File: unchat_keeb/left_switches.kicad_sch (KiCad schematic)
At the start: 54 parts

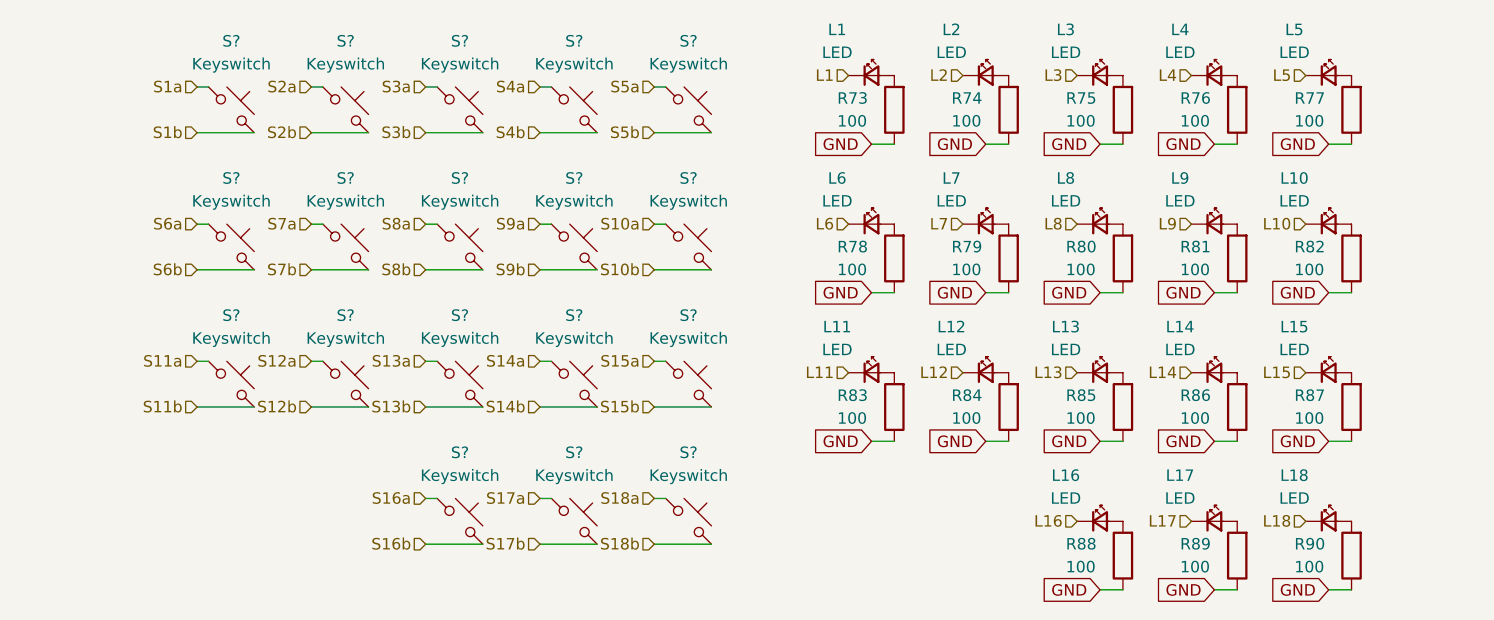
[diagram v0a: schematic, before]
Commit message: Add extra columns, updating to 42-key design
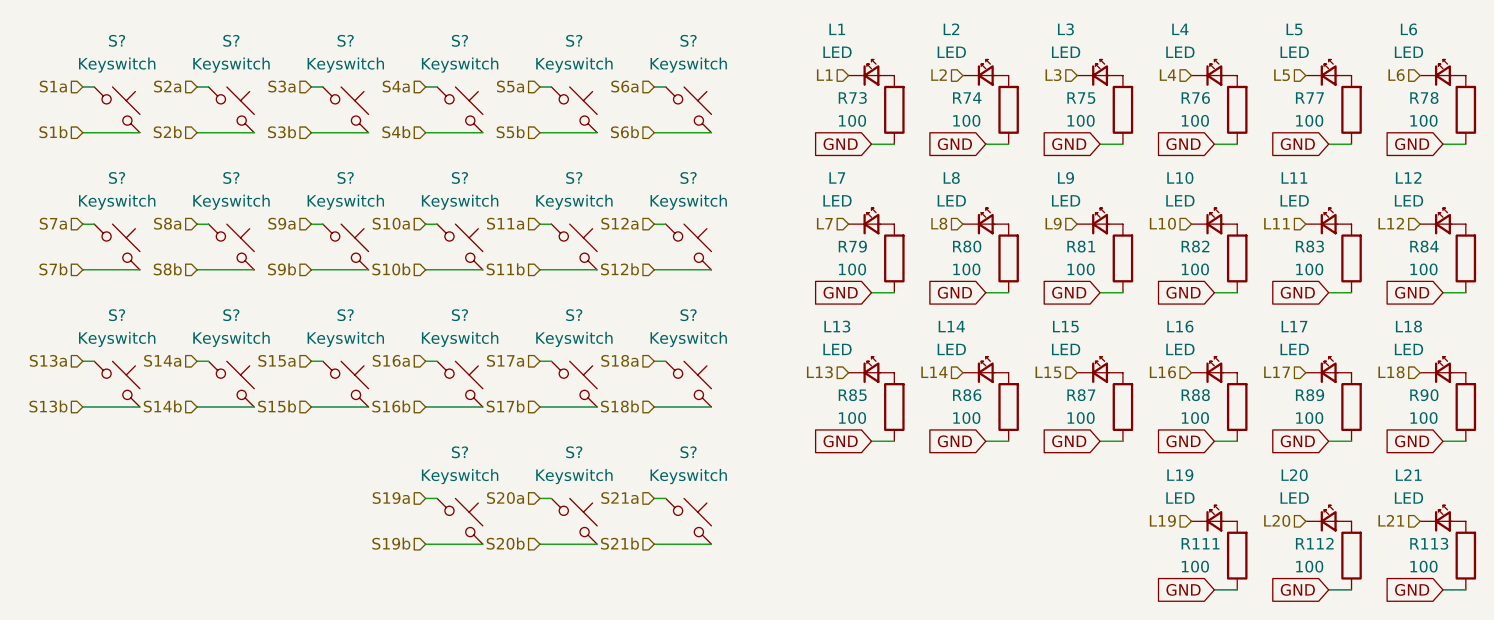
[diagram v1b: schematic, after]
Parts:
- added L1, L13, L7: LED, LED_SMD:LED_0603_1608Metric, symbol Device:LED_Small
- added R73, R79, R85: 100, Resistor_SMD:R_0805_2012Metric, symbol ScottoKeebs:Placeholder_Resistor
- added S? (x3): Keyswitch, GKanwarLibrary:Choc_V1_LED_1.00u, symbol ScottoKeebs:Placeholder_Keyswitch
- renumbered L8 to L10, L9 to L11, L10 to L12, L11 to L14, L12 to L15, L13 to L16, L14 to L17, L15 to L18, L16 to L19, L1 to L2, L17 to L20, L18 to L21, L2 to L3, L3 to L4, L4 to L5, L5 to L6, L6 to L8, L7 to L9, R88 to R111, R89 to R112, R90 to R113, R73 to R74, R74 to R75, R75 to R76, R76 to R77, R77 to R78, R78 to R80, R79 to R81, R80 to R82, R81 to R83, R82 to R84, R83 to R86, R84 to R87, R85 to R88, R86 to R89, R87 to R90
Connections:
- net GND: now also R73.1, R79.1, R85.1
- net L1: now also L1.1 (K); no longer L2.1 (K)
- net L10: now also L10.1 (K); no longer L12.1 (K)
- net L11: now also L11.1 (K); no longer L14.1 (K)
- net L12: now also L12.1 (K); no longer L15.1 (K)
- net L13: now also L13.1 (K); no longer L16.1 (K)
- net L14: now also L14.1 (K); no longer L17.1 (K)
- net L15: now also L15.1 (K); no longer L18.1 (K)
- net L16: now also L16.1 (K); no longer L19.1 (K)
- net L17: now also L17.1 (K); no longer L20.1 (K)
- net L18: now also L18.1 (K); no longer L21.1 (K)
- net L2: now also L2.1 (K); no longer L3.1 (K)
- net L3: now also L3.1 (K); no longer L4.1 (K)
- net L4: now also L4.1 (K); no longer L5.1 (K)
- net L5: now also L5.1 (K); no longer L6.1 (K)
- net L6: now also L6.1 (K); no longer L8.1 (K)
- net L7: now also L7.1 (K); no longer L9.1 (K)
- net L8: now also L8.1 (K); no longer L10.1 (K)
- net L9: now also L9.1 (K); no longer L11.1 (K)
- net S10a: now also S?.1; no longer S?.1
- net S10b: now also S?.2; no longer S?.2
- net S11a: now also S?.1; no longer S?.1
- net S11b: now also S?.2; no longer S?.2
- net S12a: now also S?.1; no longer S?.1
- net S12b: now also S?.2; no longer S?.2
- net S13a: now also S?.1; no longer S?.1
- net S13b: now also S?.2; no longer S?.2
- net S14a: now also S?.1; no longer S?.1
- net S14b: now also S?.2; no longer S?.2
- net S15a: now also S?.1; no longer S?.1
- net S15b: now also S?.2; no longer S?.2
- net S16a: now also S?.1; no longer S?.1
- net S16b: now also S?.2; no longer S?.2
- net S17a: now also S?.1; no longer S?.1
- net S17b: now also S?.2; no longer S?.2
- net S18a: now also S?.1; no longer S?.1
- net S18b: now also S?.2; no longer S?.2
- net S1a: now also S?.1; no longer S?.1
- net S1b: now also S?.2; no longer S?.2
- net S2a: now also S?.1; no longer S?.1
- net S2b: now also S?.2; no longer S?.2
- net S3a: now also S?.1; no longer S?.1
- net S3b: now also S?.2; no longer S?.2
- net S4a: now also S?.1; no longer S?.1
- net S4b: now also S?.2; no longer S?.2
- net S5a: now also S?.1; no longer S?.1
- net S5b: now also S?.2; no longer S?.2
- net S6a: now also S?.1; no longer S?.1
- net S6b: now also S?.2; no longer S?.2
- net S7a: now also S?.1; no longer S?.1
- net S7b: now also S?.2; no longer S?.2
- net S8a: now also S?.1; no longer S?.1
- net S8b: now also S?.2; no longer S?.2
- net S9a: now also S?.1; no longer S?.1
- net S9b: now also S?.2; no longer S?.2
- new net: L7.2 (A), R79.2
- new net: L1.2 (A), R73.2
- new net: L13.2 (A), R85.2
- new net L19: L19.1 (K)
- new net L20: L20.1 (K)
- new net L21: L21.1 (K)
- new net S19a: S?.1
- new net S19b: S?.2
- new net S20a: S?.1
- new net S20b: S?.2
- new net S21a: S?.1
- new net S21b: S?.2
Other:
- moved on the sheet: L10, L11, L12, L14, L15, L16, L17, L18, L19, L2, L20, L21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

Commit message: readme: Added with many images and a snippet of the timelapse
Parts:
- gave numbers to parts that had none: 21
